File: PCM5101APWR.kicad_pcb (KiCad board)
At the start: 2 copper layers, 81 x 48.4 mm, 1 part, among them U1 PCM5101A

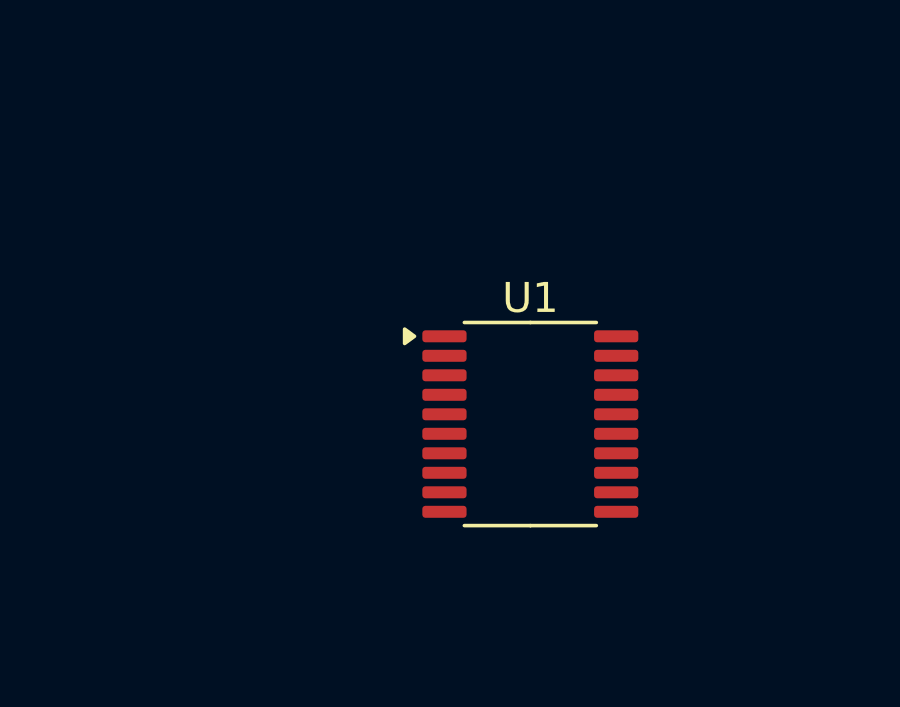
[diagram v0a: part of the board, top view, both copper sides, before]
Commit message: Added more connectors
Version change from 8 to 9
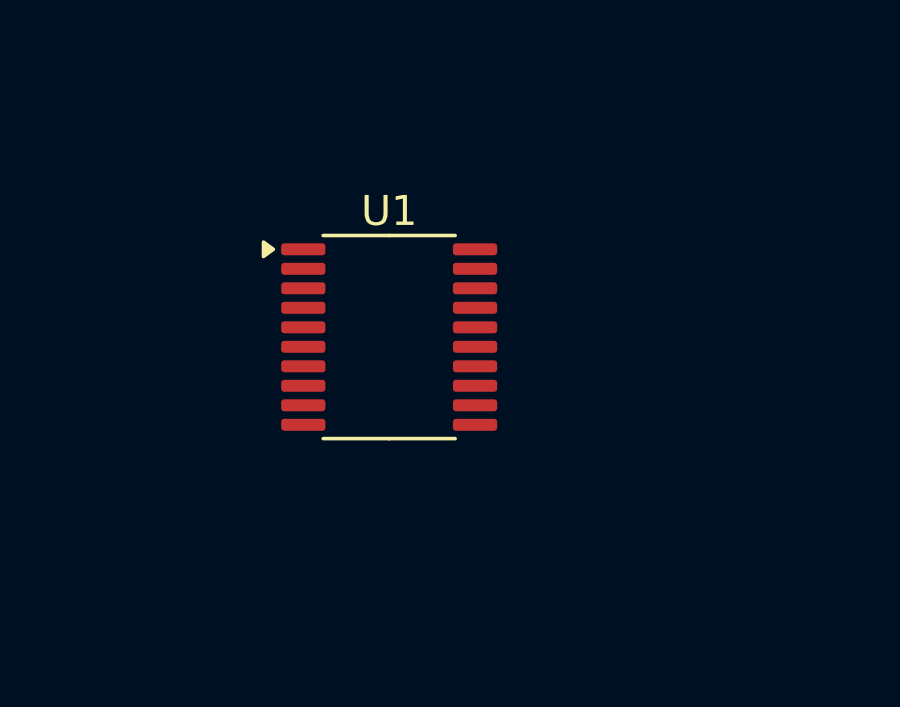
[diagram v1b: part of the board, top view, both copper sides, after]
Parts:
- moved U1 5.53 mm to (132.4, 87.1)
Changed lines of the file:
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@@
 (kicad_pcb
-	(version 20240108)
+	(version 20241229)
 	(generator "pcbnew")
-	(generator_version "8.0")
+	(generator_version "9.0")
 	(general
 		(thickness 1.6)
@@
 	(layers
 		(0 "F.Cu" signal)
-		(31 "B.Cu" signal)
-		(32 "B.Adhes" user "B.Adhesive")
-		(33 "F.Adhes" user "F.Adhesive")
-		(34 "B.Paste" user)
-		(35 "F.Paste" user)
-		(36 "B.SilkS" user "B.Silkscreen")
-		(37 "F.SilkS" user "F.Silkscreen")
-		(38 "B.Mask" user)
-		(39 "F.Mask" user)
-		(40 "Dwgs.User" user "User.Drawings")
-		(41 "Cmts.User" user "User.Comments")
-		(42 "Eco1.User" user "User.Eco1")
-		(43 "Eco2.User" user "User.Eco2")
-		(44 "Edge.Cuts" user)
-		(45 "Margin" user)
-		(46 "B.CrtYd" user "B.Courtyard")
-		(47 "F.CrtYd" user "F.Courtyard")
-		(48 "B.Fab" user)
-		(49 "F.Fab" user)
-		(50 "User.1" user)
-		(51 "User.2" user)
-		(52 "User.3" user)
-		(53 "User.4" user)
-		(54 "User.5" user)
-		(55 "User.6" user)
-		(56 "User.7" user)
-		(57 "User.8" user)
-		(58 "User.9" user)
+		(2 "B.Cu" signal)
+		(9 "F.Adhes" user "F.Adhesive")
+		(11 "B.Adhes" user "B.Adhesive")
+		(13 "F.Paste" user)
+		(15 "B.Paste" user)
+		(5 "F.SilkS" user "F.Silkscreen")
+		(7 "B.SilkS" user "B.Silkscreen")
+		(1 "F.Mask" user)
+		(3 "B.Mask" user)
+		(17 "Dwgs.User" user "User.Drawings")
+		(19 "Cmts.User" user "User.Comments")
+		(21 "Eco1.User" user "User.Eco1")
+		(23 "Eco2.User" user "User.Eco2")
+		(25 "Edge.Cuts" user)
+		(27 "Margin" user)
+		(31 "F.CrtYd" user "F.Courtyard")
+		(29 "B.CrtYd" user "B.Courtyard")
+		(35 "F.Fab" user)
+		(33 "B.Fab" user)
+		(39 "User.1" user)
+		(41 "User.2" user)
+		(43 "User.3" user)
+		(45 "User.4" user)
+		(47 "User.5" user)
+		(49 "User.6" user)
+		(51 "User.7" user)
+		(53 "User.8" user)
+		(55 "User.9" user)
 	)
 	(setup
 		(pad_to_mask_clearance 0)
 		(allow_soldermask_bridges_in_footprints no)
+		(tenting front back)
 		(pcbplotparams
-			(layerselection 0x00010fc_ffffffff)
-			(plot_on_all_layers_selection 0x0000000_00000000)
+			(layerselection 0x00000000_00000000_55555555_5755f5ff)
+			(plot_on_all_layers_selection 0x00000000_00000000_00000000_00000000)
 			(disableapertmacros no)
 			(usegerberextensions no)
@@
 			(svgprecision 4)
 			(plotframeref no)
-			(viasonmask no)
 			(mode 1)
 			(useauxorigin no)
@@
 			(pdf_front_fp_property_popups yes)
 			(pdf_back_fp_property_popups yes)
+			(pdf_metadata yes)
+			(pdf_single_document no)
 			(dxfpolygonmode yes)
 			(dxfimperialunits yes)
@@
 			(psnegative no)
 			(psa4output no)
-			(plotreference yes)
-			(plotvalue yes)
-			(plotfptext yes)
-			(plotinvisibletext no)
+			(plot_black_and_white yes)
 			(sketchpadsonfab no)
+			(plotpadnumbers no)
+			(hidednponfab no)
+			(sketchdnponfab yes)
+			(crossoutdnponfab yes)
 			(subtractmaskfromsilk no)
 			(outputformat 1)
@@
 	(footprint "Package_SO:TSSOP-20_4.4x6.5mm_P0.65mm"
 		(layer "F.Cu")
-		(at 137.0675 89.975)
+		(at 132.3625 87.075)
 		(descr "TSSOP, 20 Pin (JEDEC MO-153 Var AC https://www.jedec.org/document_search?search_api_views_fulltext=MO-153), generated with kicad-footprint-generator ipc_gullwing_generator.py")
 		(tags "TSSOP SO")
@@
 			)
 		)
-		(property "Footprint" "Package_SO:TSSOP-20_4.4x6.5mm_P0.65mm"
+		(property "Datasheet" "https://www.ti.com/lit/ds/symlink/pcm5101a.pdf"
 			(at 0 0 0)
 			(unlocked yes)
@@
 			)
 		)
-		(property "Datasheet" "https://www.ti.com/lit/ds/symlink/pcm5101a.pdf"
+		(property "Description" "2.1 VRMS, 106dB Audio Stereo DAC with PLL and 32-bit, 384kHz PCM Interface, TSSOP-20"
 			(at 0 0 0)
 			(unlocked yes)
@@
 			)
 		)
-		(property "Description" "2.1 VRMS, 106dB Audio Stereo DAC with PLL and 32-bit, 384kHz PCM Interface, TSSOP-20"
-			(at 0 0 0)
-			(unlocked yes)
-			(layer "F.Fab")
-			(hide yes)
-			(effects
-				(font
-					(size 1.27 1.27)
-					(thickness 0.15)
-				)
-			)
-		)
 		(property ki_fp_filters "TSSOP*4.4x6.5mm*P0.65mm*")
 		(sheetname "Root")
@@
 				(type solid)
 			)
-			(fill solid)
+			(fill yes)
 			(layer "F.SilkS")
 		)
@@
 			(at -2.8625 -2.925)
 			(size 1.475 0.4)
-			(layers "F.Cu" "F.Paste" "F.Mask")
+			(layers "F.Cu" "F.Mask" "F.Paste")
 			(roundrect_rratio 0.25)
 			(net 10 "unconnected-(U1-CPVDD-Pad1)")
@@
 			(at -2.8625 -2.275)
 			(size 1.475 0.4)
-			(layers "F.Cu" "F.Paste" "F.Mask")
+			(layers "F.Cu" "F.Mask" "F.Paste")
 			(roundrect_rratio 0.25)
 			(net 16 "unconnected-(U1-CAPP-Pad2)")
@@
 			(at -2.8625 -1.625)
 			(size 1.475 0.4)
-			(layers "F.Cu" "F.Paste" "F.Mask")
+			(layers "F.Cu" "F.Mask" "F.Paste")
 			(roundrect_rratio 0.25)
 			(net 1 "GND")
@@
 			(at -2.8625 -0.975)
 			(size 1.475 0.4)
-			(layers "F.Cu" "F.Paste" "F.Mask")
+			(layers "F.Cu" "F.Mask" "F.Paste")
 			(roundrect_rratio 0.25)
 			(net 6 "unconnected-(U1-CAPM-Pad4)")
@@
 			(at -2.8625 -0.325)
 			(size 1.475 0.4)
-			(layers "F.Cu" "F.Paste" "F.Mask")
+			(layers "F.Cu" "F.Mask" "F.Paste")
 			(roundrect_rratio 0.25)
 			(net 7 "unconnected-(U1-VNEG-Pad5)")
@@
 			(at -2.8625 0.325)
 			(size 1.475 0.4)
-			(layers "F.Cu" "F.Paste" "F.Mask")
+			(layers "F.Cu" "F.Mask" "F.Paste")
 			(roundrect_rratio 0.25)
 			(net 18 "unconnected-(U1-OUTL-Pad6)")
@@
 			(at -2.8625 0.975)
 			(size 1.475 0.4)
-			(layers "F.Cu" "F.Paste" "F.Mask")
+			(layers "F.Cu" "F.Mask" "F.Paste")
 			(roundrect_rratio 0.25)
 			(net 13 "unconnected-(U1-OUTR-Pad7)")
@@
 			(at -2.8625 1.625)
 			(size 1.475 0.4)
-			(layers "F.Cu" "F.Paste" "F.Mask")
+			(layers "F.Cu" "F.Mask" "F.Paste")
 			(roundrect_rratio 0.25)
 			(net 12 "unconnected-(U1-AVDD-Pad8)")
@@
 			(at -2.8625 2.275)
 			(size 1.475 0.4)
-			(layers "F.Cu" "F.Paste" "F.Mask")
+			(layers "F.Cu" "F.Mask" "F.Paste")
 			(roundrect_rratio 0.25)
 			(net 1 "GND")
@@
 			(at -2.8625 2.925)
 			(size 1.475 0.4)
-			(layers "F.Cu" "F.Paste" "F.Mask")
+			(layers "F.Cu" "F.Mask" "F.Paste")
 			(roundrect_rratio 0.25)
 			(net 4 "unconnected-(U1-DEMP-Pad10)")
@@
 			(at 2.8625 2.925)
 			(size 1.475 0.4)
-			(layers "F.Cu" "F.Paste" "F.Mask")
+			(layers "F.Cu" "F.Mask" "F.Paste")
 			(roundrect_rratio 0.25)
 			(net 14 "unconnected-(U1-FLT-Pad11)")
@@
 			(at 2.8625 2.275)
 			(size 1.475 0.4)
-			(layers "F.Cu" "F.Paste" "F.Mask")
+			(layers "F.Cu" "F.Mask" "F.Paste")
 			(roundrect_rratio 0.25)
 			(net 15 "unconnected-(U1-SCK-Pad12)")
@@
 			(at 2.8625 1.625)
 			(size 1.475 0.4)
-			(layers "F.Cu" "F.Paste" "F.Mask")
+			(layers "F.Cu" "F.Mask" "F.Paste")
 			(roundrect_rratio 0.25)
 			(net 5 "unconnected-(U1-BCK-Pad13)")
@@
 			(at 2.8625 0.975)
 			(size 1.475 0.4)
-			(layers "F.Cu" "F.Paste" "F.Mask")
+			(layers "F.Cu" "F.Mask" "F.Paste")
 			(roundrect_rratio 0.25)
 			(net 11 "unconnected-(U1-DIN-Pad14)")
@@
 			(at 2.8625 0.325)
 			(size 1.475 0.4)
-			(layers "F.Cu" "F.Paste" "F.Mask")
+			(layers "F.Cu" "F.Mask" "F.Paste")
 			(roundrect_rratio 0.25)
 			(net 3 "unconnected-(U1-LRCK-Pad15)")
@@
 			(at 2.8625 -0.325)
 			(size 1.475 0.4)
-			(layers "F.Cu" "F.Paste" "F.Mask")
+			(layers "F.Cu" "F.Mask" "F.Paste")
 			(roundrect_rratio 0.25)
 			(net 8 "unconnected-(U1-FMT-Pad16)")
@@
 			(at 2.8625 -0.975)
 			(size 1.475 0.4)
-			(layers "F.Cu" "F.Paste" "F.Mask")
+			(layers "F.Cu" "F.Mask" "F.Paste")
 			(roundrect_rratio 0.25)
 			(net 9 "unconnected-(U1-XSMT-Pad17)")
@@
 			(at 2.8625 -1.625)
 			(size 1.475 0.4)
-			(layers "F.Cu" "F.Paste" "F.Mask")
+			(layers "F.Cu" "F.Mask" "F.Paste")
 			(roundrect_rratio 0.25)
 			(net 2 "unconnected-(U1-LDOO-Pad18)")
@@
 			(at 2.8625 -2.275)
 			(size 1.475 0.4)
-			(layers "F.Cu" "F.Paste" "F.Mask")
+			(layers "F.Cu" "F.Mask" "F.Paste")
 			(roundrect_rratio 0.25)
 			(net 1 "GND")
@@
 			(at 2.8625 -2.925)
 			(size 1.475 0.4)
-			(layers "F.Cu" "F.Paste" "F.Mask")
+			(layers "F.Cu" "F.Mask" "F.Paste")
 			(roundrect_rratio 0.25)
 			(net 17 "unconnected-(U1-DVDD-Pad20)")
@@
 			(pintype "power_in")
 		)
+		(embedded_fonts no)
 		(model "${KICAD8_3DMODEL_DIR}/Package_SO.3dshapes/TSSOP-20_4.4x6.5mm_P0.65mm.wrl"
 			(offset
@@
 			(type default)
 		)
-		(fill none)
+		(fill no)
 		(layer "Edge.Cuts")
 	)
+	(embedded_fonts no)
 )

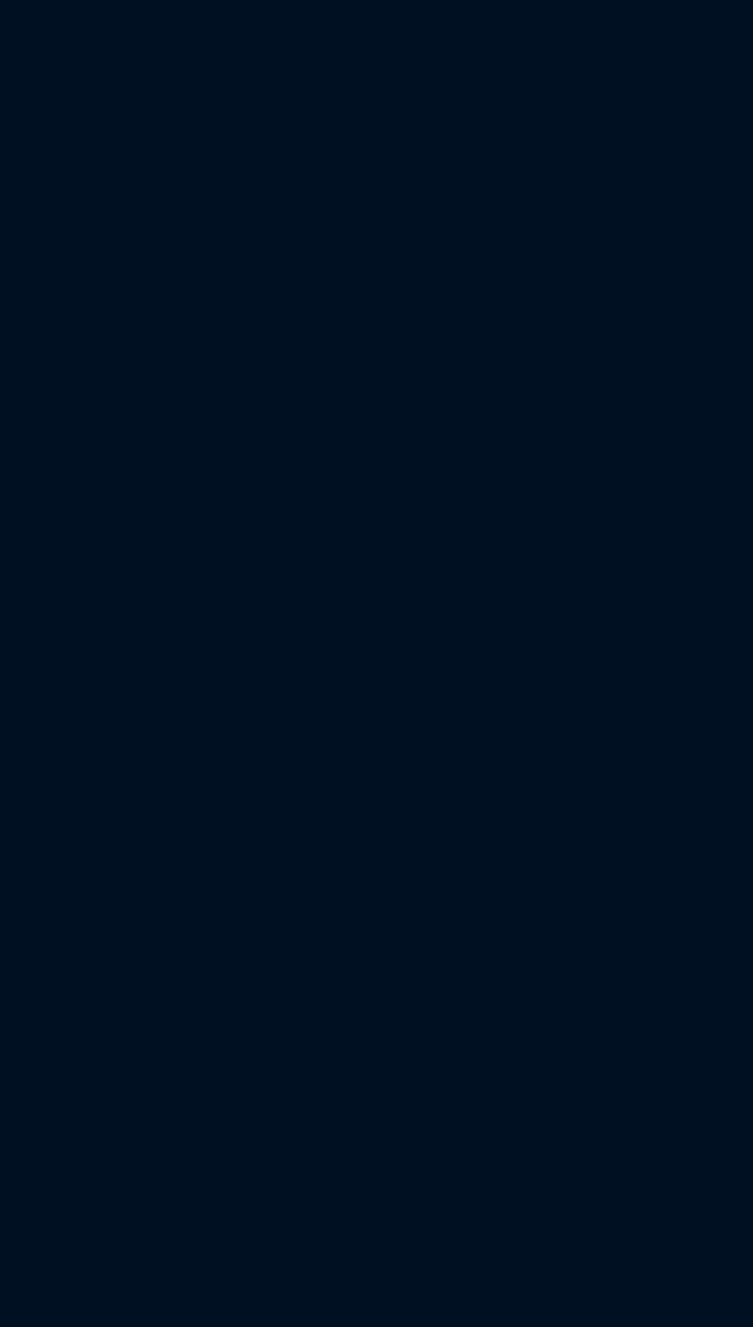
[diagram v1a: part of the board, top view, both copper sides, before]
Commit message: eco'ed to pcb
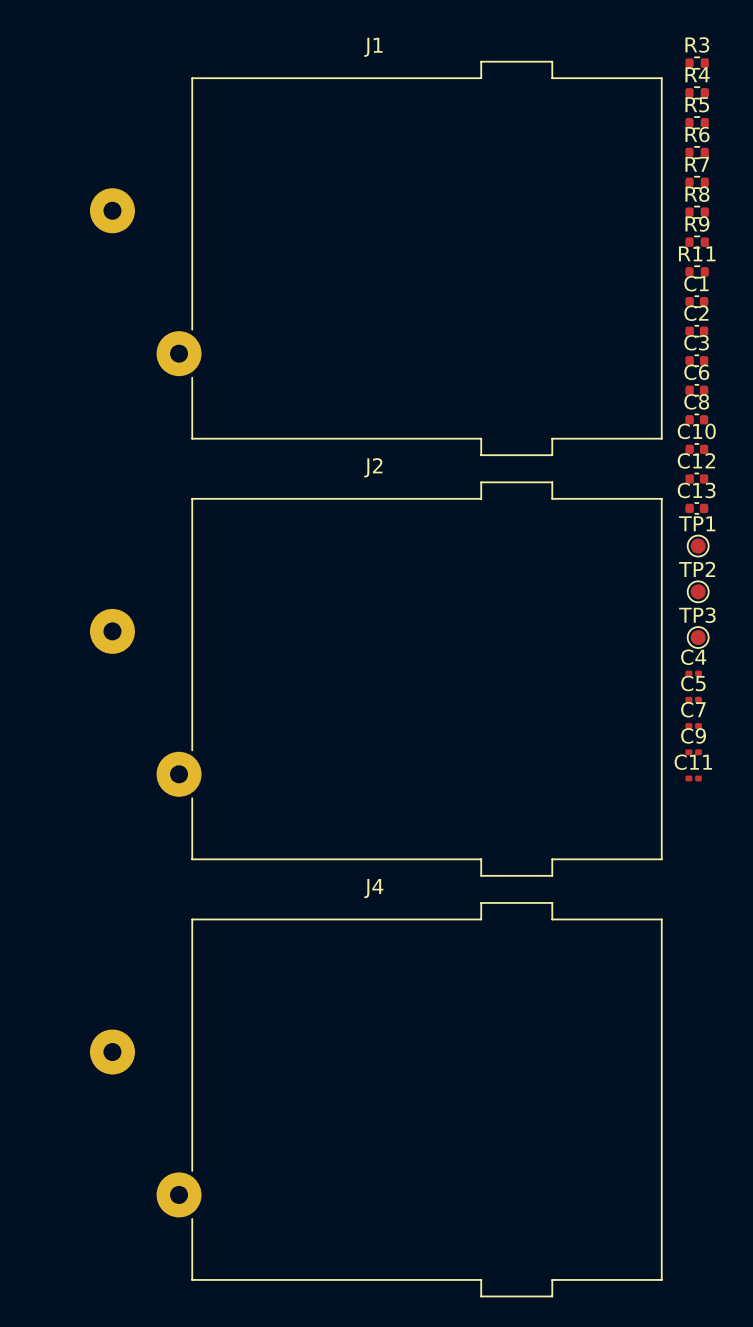
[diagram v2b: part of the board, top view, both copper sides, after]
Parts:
- added C1: 2.2n, Capacitor_SMD:C_0402_1005Metric, F.Cu at (240.9, 65.7)
- added C10: 100n, Capacitor_SMD:C_0402_1005Metric, F.Cu at (240.9, 75.5)
- added C11: 2.2u, Capacitor_SMD:C_0201_0603Metric, F.Cu at (240.7, 97.5)
- added C12: 2.2n, Capacitor_SMD:C_0402_1005Metric, F.Cu at (240.9, 77.5)
- added C13: 2.2n, Capacitor_SMD:C_0402_1005Metric, F.Cu at (240.9, 79.5)
- added C2: 2.2n, Capacitor_SMD:C_0402_1005Metric, F.Cu at (240.9, 67.7)
- added C3: 100n, Capacitor_SMD:C_0402_1005Metric, F.Cu at (240.9, 69.6)
- added C4: 10u, Capacitor_SMD:C_0201_0603Metric, F.Cu at (240.7, 90.5)
- added C5: 10u, Capacitor_SMD:C_0201_0603Metric, F.Cu at (240.7, 92.2)
- added C6: 100n, Capacitor_SMD:C_0402_1005Metric, F.Cu at (240.9, 71.6)
- added C7: 10u, Capacitor_SMD:C_0201_0603Metric, F.Cu at (240.7, 94.0)
- added C8: 100n, Capacitor_SMD:C_0402_1005Metric, F.Cu at (240.9, 73.6)
- added C9: 2.2u, Capacitor_SMD:C_0201_0603Metric, F.Cu at (240.7, 95.8)
- added J1: AudioJack2, Connector_Audio:Jack_speakON-6.35mm_Neutrik_NLJ2MDXX-H_Horizontal, F.Cu at (201.9, 59.6)
- added J2: AudioJack2, Connector_Audio:Jack_speakON-6.35mm_Neutrik_NLJ2MDXX-H_Horizontal, F.Cu at (201.9, 87.7)
- added J4: AudioJack2, Connector_Audio:Jack_speakON-6.35mm_Neutrik_NLJ2MDXX-H_Horizontal, F.Cu at (201.9, 115.7)
- added R11: 0, Resistor_SMD:R_0402_1005Metric, F.Cu at (240.9, 63.7)
- added R3: 0, Resistor_SMD:R_0402_1005Metric, F.Cu at (240.9, 49.8)
- added R4: 0, Resistor_SMD:R_0402_1005Metric, F.Cu at (240.9, 51.8)
- added R5: 0, Resistor_SMD:R_0402_1005Metric, F.Cu at (240.9, 53.8)
- added R6: 0, Resistor_SMD:R_0402_1005Metric, F.Cu at (240.9, 55.8)
- added R7: 0, Resistor_SMD:R_0402_1005Metric, F.Cu at (240.9, 57.8)
- added R8: 0, Resistor_SMD:R_0402_1005Metric, F.Cu at (240.9, 59.7)
- added R9: 0, Resistor_SMD:R_0402_1005Metric, F.Cu at (240.9, 61.7)
- added TP1: TestPoint, TestPoint:TestPoint_Pad_D1.0mm, F.Cu at (241.0, 82.0)
- added TP2: TestPoint, TestPoint:TestPoint_Pad_D1.0mm, F.Cu at (241.0, 85.0)
- added TP3: TestPoint, TestPoint:TestPoint_Pad_D1.0mm, F.Cu at (241.0, 88.1)
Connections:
- U1 pad 1: unconnected-(U1-CPVDD-Pad1) -> +3.3VA
- U1 pad 10: unconnected-(U1-DEMP-Pad10) -> GND
- U1 pad 11: unconnected-(U1-FLT-Pad11) -> GND
- U1 pad 12: unconnected-(U1-SCK-Pad12) -> Net-(U1-SCK)
- U1 pad 13: unconnected-(U1-BCK-Pad13) -> Net-(U1-BCK)
- U1 pad 14: unconnected-(U1-DIN-Pad14) -> Net-(U1-DIN)
- U1 pad 15: unconnected-(U1-LRCK-Pad15) -> Net-(U1-LRCK)
- U1 pad 16: unconnected-(U1-FMT-Pad16) -> GND
- U1 pad 17: unconnected-(U1-XSMT-Pad17) -> +3.3V
- U1 pad 18: unconnected-(U1-LDOO-Pad18) -> Net-(U1-LDOO)
- U1 pad 2: unconnected-(U1-CAPP-Pad2) -> Net-(U1-CAPP)
- U1 pad 20: unconnected-(U1-DVDD-Pad20) -> +3.3V
- U1 pad 4: unconnected-(U1-CAPM-Pad4) -> Net-(U1-CAPM)
- U1 pad 5: unconnected-(U1-VNEG-Pad5) -> Net-(U1-VNEG)
- U1 pad 6: unconnected-(U1-OUTL-Pad6) -> Net-(U1-OUTL)
- U1 pad 7: unconnected-(U1-OUTR-Pad7) -> Net-(U1-OUTR)
- U1 pad 8: unconnected-(U1-AVDD-Pad8) -> +3.3VA
